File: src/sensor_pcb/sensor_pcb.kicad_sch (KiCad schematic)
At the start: 29 parts, among them IC1 TCAN3414DRBR, J1 66200421024, J2 643280100305, J3 66200821024, J4 643280100305, J5 66200821024, J7 66200421024, U1 SHT45-AD1B, U2 16-bit ADC, U4 BMP581

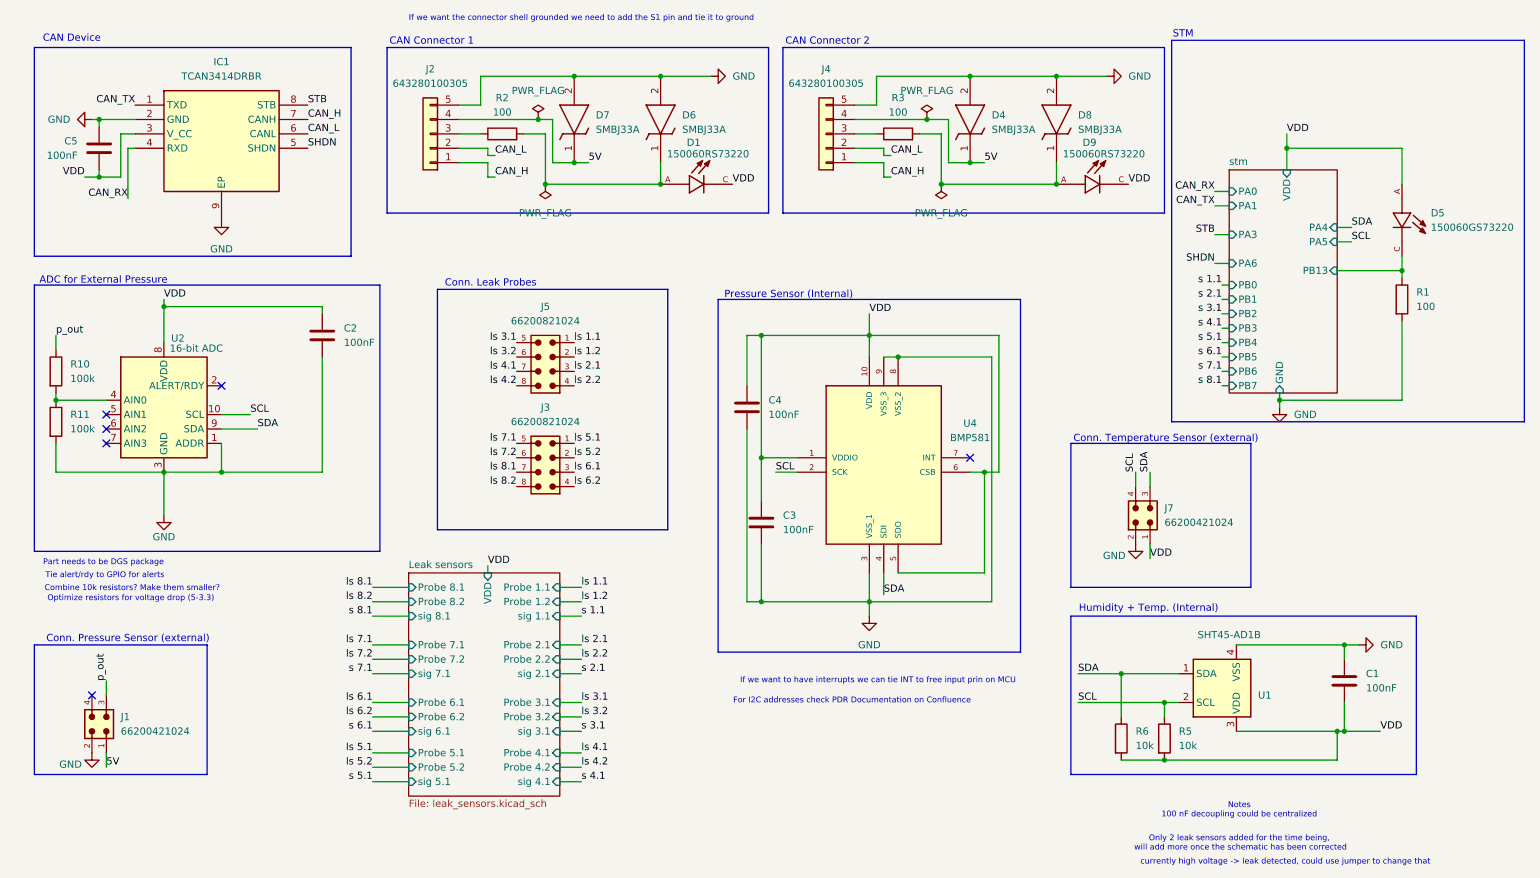
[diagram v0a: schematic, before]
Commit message: fixing up parts according to kicad auto errors
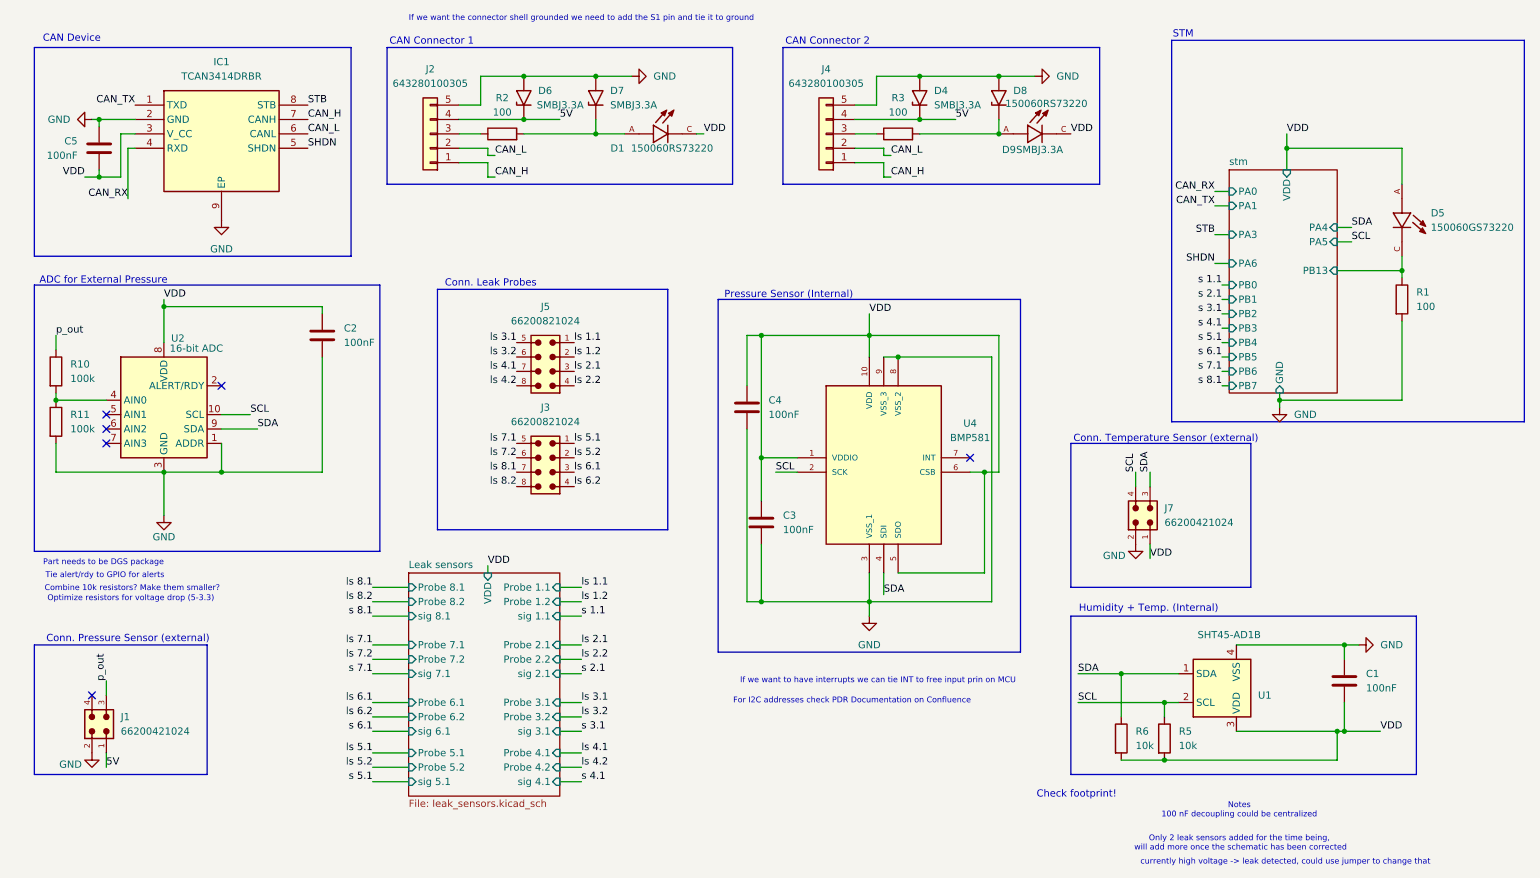
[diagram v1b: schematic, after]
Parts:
- removed D4, D6, D7, D8: SMBJ33A, DIOM5436X244N, symbol dz_dio:SMBJ33A
- added D4, D6, D7, D8: SMBJ3.3A, Diode_SMD:D_SMB, symbol #dzdb:s_dio/D-TVS-SMBJ3V3
- U4: footprint dz_sens:BMP581 -> dz_sens:QFN10_BMP581_BOS
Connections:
- net 5V: now also D4.1 (A1), D6.1 (A1)
- net GND: now also D4.2 (A2), D6.2 (A2), D7.2 (A2), D8.2 (A2)
- net at D1.A, R2.2: now also D7.1 (A1)
- net at D9.A, R3.2: now also D8.1 (A1)
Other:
- note added: "Check footprint!"
- moved on the sheet: D1, D9

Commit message: removed error messages
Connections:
- net 5V renamed +5V
- no-connect marks 6 -> 8
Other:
- sheet stm ports: added PA2, PA9; removed none
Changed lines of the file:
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@@
 	)
 	(junction
+		(at 171.45 33.02)
+		(diameter 0)
+		(color 0 0 0 0)
+	)
+	(junction
+		(at 101.6 33.02)
+		(diameter 0)
+		(color 0 0 0 0)
+	)
+	(junction
 		(at 220.98 135.89)
 		(diameter 0)
@@
 	)
 	(no_connect
+		(at 232.41 50.8)
+	)
+	(no_connect
 		(at 54.61 80.01)
 	)
@@
 	)
 	(no_connect
+		(at 251.46 63.5)
+	)
+	(no_connect
 		(at 34.29 87.63)
 	)
@@
 	(wire
 		(pts
-			(xy 96.52 33.02) (xy 107.95 33.02)
+			(xy 96.52 33.02) (xy 101.6 33.02)
 		)
 		(stroke
@@
 	(wire
 		(pts
+			(xy 101.6 33.02) (xy 107.95 33.02)
+		)
+		(stroke
+			(width 0)
+			(type default)
+		)
+	)
+	(wire
+		(pts
 			(xy 149.86 92.71) (xy 149.86 100.33)
 		)
@@
 	(wire
 		(pts
-			(xy 166.37 33.02) (xy 177.8 33.02)
+			(xy 166.37 33.02) (xy 171.45 33.02)
 		)
 		(stroke
@@
 	(wire
 		(pts
+			(xy 171.45 33.02) (xy 177.8 33.02)
+		)
+		(stroke
+			(width 0)
+			(type default)
+		)
+	)
+	(wire
+		(pts
 			(xy 72.39 95.25) (xy 54.61 95.25)
 		)
@@
 	)
 	(symbol
+		(lib_id "power:+5V")
+		(at 101.6 33.02 0)
+		(unit 1)
+		(exclude_from_sim no)
+		(in_bom yes)
+		(on_board yes)
+		(dnp no)
+		(fields_autoplaced yes)
+		(property "Reference" "#PWR020"
+			(at 101.6 36.83 0)
+			(effects
+				(font
+					(size 1.27 1.27)
+				)
+				(hide yes)
+			)
+		)
+		(property "Value" "+5V"
+			(at 101.6 27.94 0)
+			(effects
+				(font
+					(size 1.27 1.27)
+				)
+			)
+		)
+		(property "Footprint" ""
+			(at 101.6 33.02 0)
+			(effects
+				(font
+					(size 1.27 1.27)
+				)
+				(hide yes)
+			)
+		)
+		(property "Datasheet" ""
+			(at 101.6 33.02 0)
+			(effects
+				(font
+					(size 1.27 1.27)
+				)
+				(hide yes)
+			)
+		)
+		(property "Description" "Power symbol creates a global label with name \"+5V\""
+			(at 101.6 33.02 0)
+			(effects
+				(font
+					(size 1.27 1.27)
+				)
+				(hide yes)
+			)
+		)
+		(pin "1"
+		)
+		(instances
+			(project ""
+				(path "/4c8e18e1-465e-4d97-b2d1-f3fb0b3e2f0b"
+					(reference "#PWR020")
+					(unit 1)
+				)
+			)
+		)
+	)
+	(symbol
 		(lib_id "power:GND")
 		(at 127 25.4 90)
@@
 	)
 	(symbol
+		(lib_id "power:+5V")
+		(at 171.45 33.02 0)
+		(unit 1)
+		(exclude_from_sim no)
+		(in_bom yes)
+		(on_board yes)
+		(dnp no)
+		(fields_autoplaced yes)
+		(property "Reference" "#PWR019"
+			(at 171.45 36.83 0)
+			(effects
+				(font
+					(size 1.27 1.27)
+				)
+				(hide yes)
+			)
+		)
+		(property "Value" "+5V"
+			(at 171.45 27.94 0)
+			(effects
+				(font
+					(size 1.27 1.27)
+				)
+			)
+		)
+		(property "Footprint" ""
+			(at 171.45 33.02 0)
+			(effects
+				(font
+					(size 1.27 1.27)
+				)
+				(hide yes)
+			)
+		)
+		(property "Datasheet" ""
+			(at 171.45 33.02 0)
+			(effects
+				(font
+					(size 1.27 1.27)
+				)
+				(hide yes)
+			)
+		)
+		(property "Description" "Power symbol creates a global label with name \"+5V\""
+			(at 171.45 33.02 0)
+			(effects
+				(font
+					(size 1.27 1.27)
+				)
+				(hide yes)
+			)
+		)
+		(pin "1"
+		)
+		(instances
+			(project ""
+				(path "/4c8e18e1-465e-4d97-b2d1-f3fb0b3e2f0b"
+					(reference "#PWR019")
+					(unit 1)
+				)
+			)
+		)
+	)
+	(symbol
 		(lib_id "#dzdb:s_dio/D-TVS-SMBJ3V3")
 		(at 107.95 29.21 90)
@@
 			)
 		)
+		(pin "PA2" input
+			(at 232.41 50.8 180)
+			(effects
+				(font
+					(size 1.27 1.27)
+				)
+				(justify left)
+			)
+		)
+		(pin "PA9" input
+			(at 251.46 63.5 0)
+			(effects
+				(font
+					(size 1.27 1.27)
+				)
+				(justify right)
+			)
+		)

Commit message: Sensor PCB suggestion Davide
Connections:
- net GND: now also D9.C
- net at D9.A, R3.2: no longer D8.1 (A1)
- net +3.3V: now reaches J4.3 (Pin_3), R3.1
- net +3.3V: now also C1.2, C2.1, C3.1, C4.1, C5.2, D1.C, D5.A, D8.1 (A1), IC1.3 (V_CC), J7.1, R5.2, R6.2, U1.3 (VDD), U2.8 (VDD), U4.1 (VDDIO), U4.10 (VDD), U4.5 (SDO), U4.6 (CSB)
- removed net VDD: C1.2, C2.1, C3.1, C4.1, C5.2, D1.C, D5.A, D9.C, IC1.3 (V_CC), J7.1, R5.2, R6.2, U1.3 (VDD), U2.8 (VDD), U4.1 (VDDIO), U4.10 (VDD), U4.5 (SDO), U4.6 (CSB)
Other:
- moved on the sheet: C2, C3, C4, D9, R3

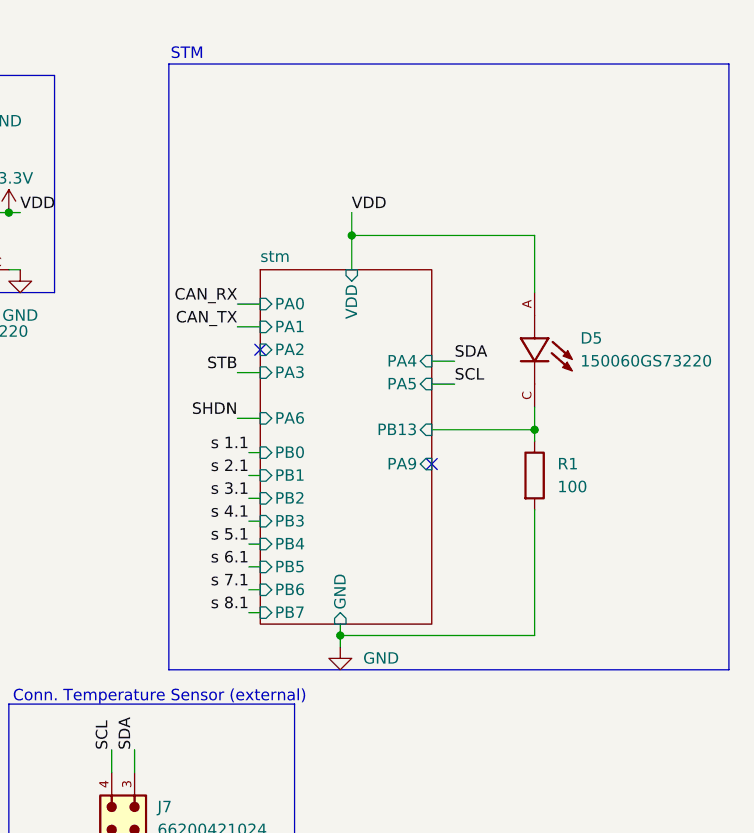
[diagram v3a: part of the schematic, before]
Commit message: added stm
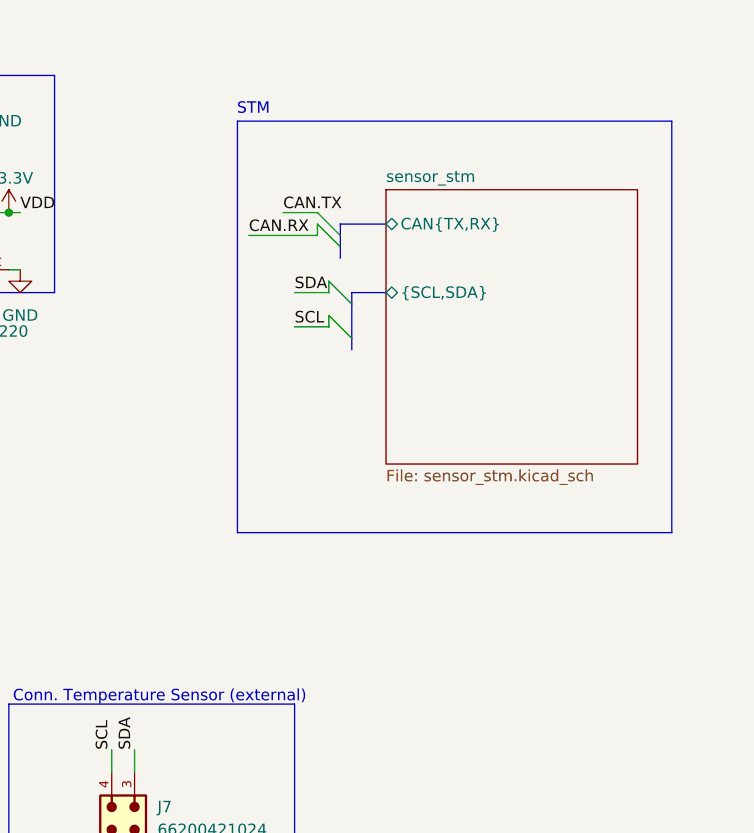
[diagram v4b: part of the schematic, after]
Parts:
- removed D5: 150060GS73220, dz_dio:LED_0603, symbol #dzdb:s_dio/D-WUR-150060GS73220
- removed R1: 100, Resistor_SMD:R_0402_1005Metric, symbol #dzdb:g_res/R-100-0402
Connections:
- no-connect marks 8 -> 6
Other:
- removed sheet stm
- added sheet sensor_stm (sensor_stm.kicad_sch)
